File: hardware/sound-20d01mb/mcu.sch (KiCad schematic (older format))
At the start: 21 parts

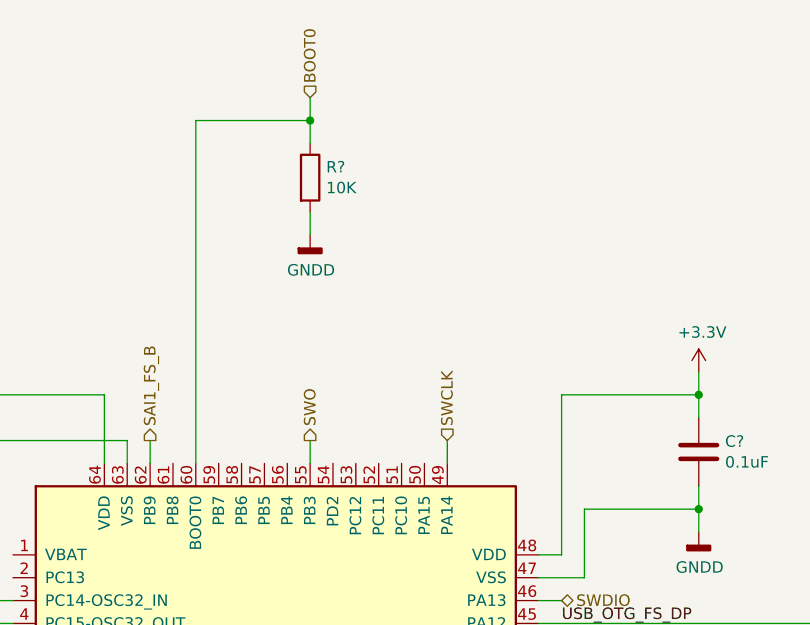
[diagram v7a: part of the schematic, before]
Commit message: Added I2C Volume control
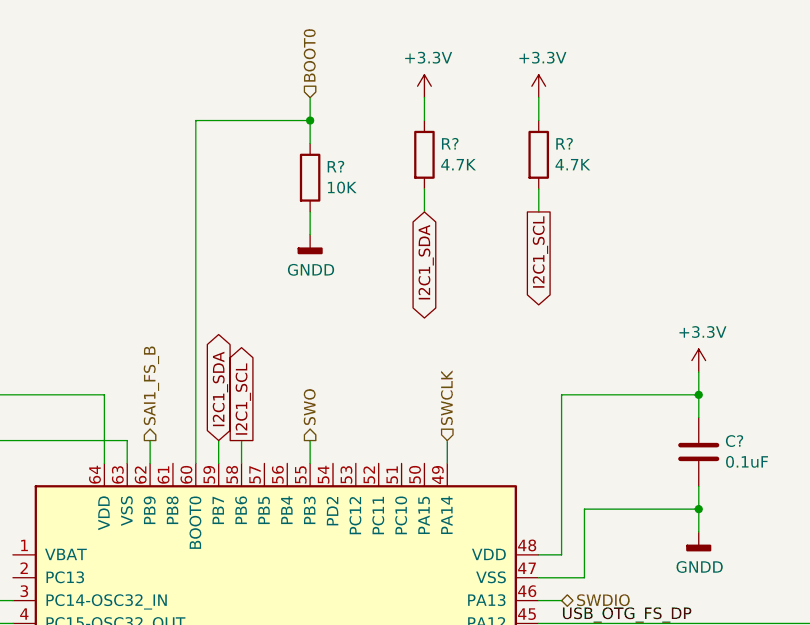
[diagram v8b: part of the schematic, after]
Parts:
- added R? (x2): 4.7K, Resistor_SMD:R_1206_3216Metric_Pad1.42x1.75mm_HandSolder, symbol Device:R
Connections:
- net +3V3: now also R?.1, R?.1
- net I2C1_SCL: now reaches U?.58 (PB6)
- net I2C1_SCL: now also R?.2
- net I2C1_SDA: now reaches U?.59 (PB7)
- net I2C1_SDA: now also R?.2
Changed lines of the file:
@@
 Wire Wire Line
 	8450 4650 8550 4650
+Wire Wire Line
+	5150 2500 5150 2400
+Wire Wire Line
+	5050 2500 5050 2400
+Text GLabel 5050 2400 1    50   BiDi ~ 0
+I2C1_SDA
+Text GLabel 5150 2400 1    50   Output ~ 0
+I2C1_SCL
+Text GLabel 5950 1400 3    50   BiDi ~ 0
+I2C1_SDA
+Text GLabel 6450 1400 3    50   Output ~ 0
+I2C1_SCL
+$Comp
+L Device:R R?
+U 1 1 6147BEB3
+P 5950 1150
+F 0 "R?" H 6020 1196 50  0000 L CNN
+F 1 "4.7K" H 6020 1105 50  0000 L CNN
+F 2 "Resistor_SMD:R_1206_3216Metric_Pad1.42x1.75mm_HandSolder" V 5880 1150 50  0001 C CNN
+F 3 "~" H 5950 1150 50  0001 C CNN
+	1    5950 1150
+	1    0    0    -1
+$EndComp
+Wire Wire Line
+	5950 1300 5950 1400
+Wire Wire Line
+	5950 900  5950 1000
+$Comp
+L power:+3.3V #PWR?
+U 1 1 6147FF35
+P 5950 900
+F 0 "#PWR?" H 5950 750 50  0001 C CNN
+F 1 "+3.3V" H 5965 1073 50  0000 C CNN
+F 2 "" H 5950 900 50  0001 C CNN
+F 3 "" H 5950 900 50  0001 C CNN
+	1    5950 900
+	1    0    0    -1
+$EndComp
+$Comp
+L Device:R R?
+U 1 1 6148000C
+P 6450 1150
+F 0 "R?" H 6520 1196 50  0000 L CNN
+F 1 "4.7K" H 6520 1105 50  0000 L CNN
+F 2 "Resistor_SMD:R_1206_3216Metric_Pad1.42x1.75mm_HandSolder" V 6380 1150 50  0001 C CNN
+F 3 "~" H 6450 1150 50  0001 C CNN
+	1    6450 1150
+	1    0    0    -1
+$EndComp
+Wire Wire Line
+	6450 1300 6450 1400
+Wire Wire Line
+	6450 900  6450 1000
+$Comp
+L power:+3.3V #PWR?
+U 1 1 61480014
+P 6450 900
+F 0 "#PWR?" H 6450 750 50  0001 C CNN
+F 1 "+3.3V" H 6465 1073 50  0000 C CNN
+F 2 "" H 6450 900 50  0001 C CNN
+F 3 "" H 6450 900 50  0001 C CNN
+	1    6450 900
+	1    0    0    -1
+$EndComp
 $EndSCHEMATC
